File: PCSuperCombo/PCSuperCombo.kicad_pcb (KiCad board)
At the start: 2 copper layers, 123.3 x 95 mm, 44 parts, among them CN1 DB9 Male, J1 IDE_CONNECTOR, J2 CF Adapter Power, J3 Bus_ISA_8bit, J4 LED, SW1 Options, U1 BIOS FLASH, U10 1.8432 MHz, U2 74HCT245, U3 ATF/GAL16V8x-15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

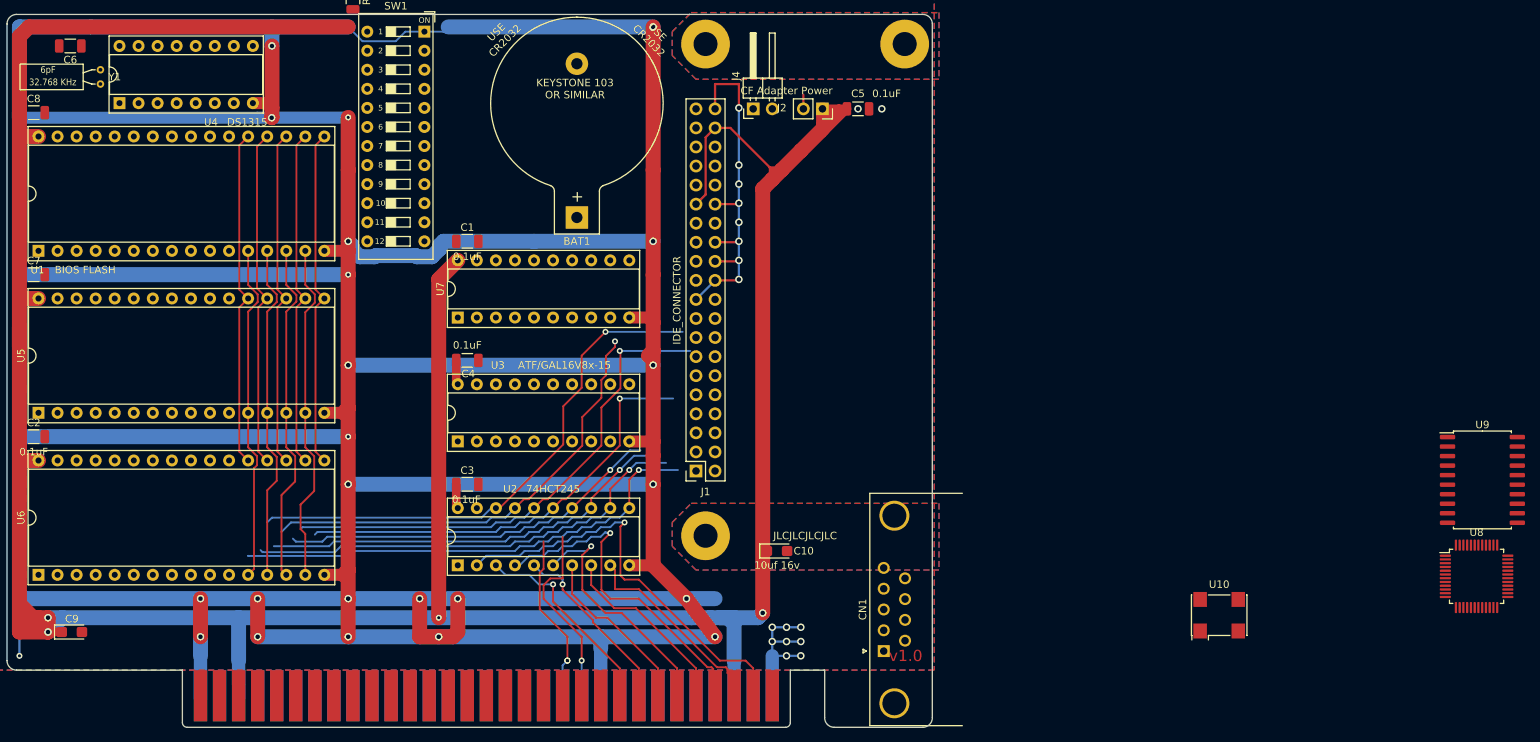
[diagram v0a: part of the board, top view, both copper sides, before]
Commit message: Committing some old edits from mid-2022 to PCSuperCombo. Not sure if these are good changes that should be comitted.
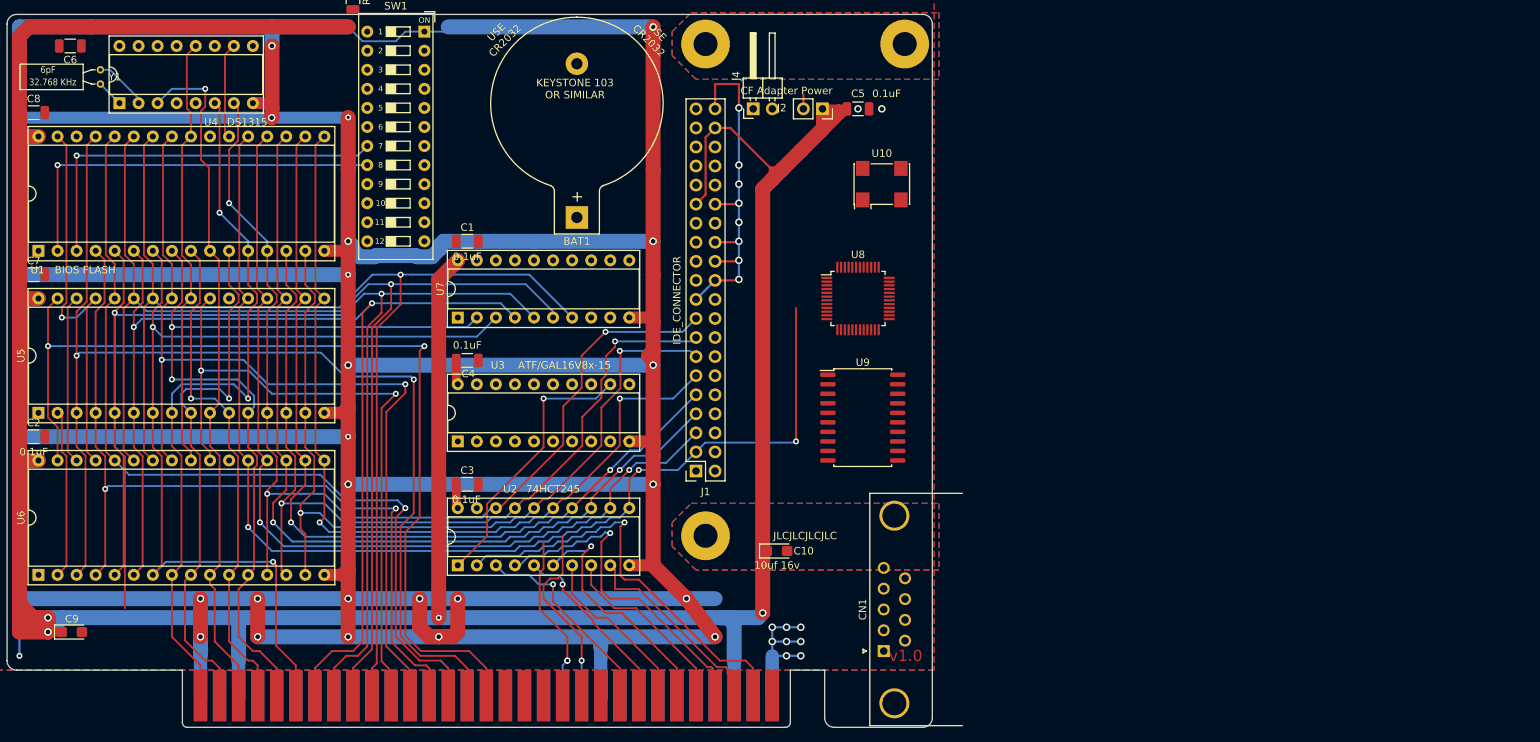
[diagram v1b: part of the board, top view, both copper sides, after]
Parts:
- moved U8 90.4 mm to (186.7, 85.1)
- moved U9 83.0 mm to (187.3, 101.0)
- moved U10 73.0 mm to (189.9, 69.8)
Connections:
- U1 pad 13: Net-(U1-Pad13) -> D0_BUF
- U1 pad 14: Net-(U1-Pad14) -> D1_BUF
- U1 pad 15: Net-(U1-Pad15) -> D2_BUF
- U1 pad 17: Net-(U1-Pad17) -> D3_BUF
- U1 pad 18: Net-(U1-Pad18) -> D4_BUF
- U1 pad 19: Net-(U1-Pad19) -> D5_BUF
- U1 pad 20: Net-(U1-Pad20) -> D6_BUF
- U1 pad 21: Net-(U1-Pad21) -> D7_BUF
- U5 pad 11: A01 -> A03
- U5 pad 12: A00 -> A04
- U5 pad 8: A04 -> A00
- U5 pad 9: A03 -> A01
- U6 pad 11: A01 -> A03
- U6 pad 12: A00 -> A04
- U6 pad 8: A04 -> A00
- U6 pad 9: A03 -> A01
- Y1 pad 1: /XTAL1 -> /XTAL2
- Y1 pad 2: /XTAL2 -> /XTAL1
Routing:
- net A07: track 0.00 -> 200.7 mm, vias 0 -> 2
- net A09: track 0.00 -> 163.4 mm, vias 0 -> 1
- net A08: track 0.25 -> 162.9 mm, vias 0 -> 1
- net A14: track 0.00 -> 156.3 mm, vias 0 -> 2
- net A06: track 0.00 -> 155.1 mm, vias 0 -> 2
- net A15: track 0.00 -> 128.7 mm, vias 0 -> 2
- net A05: track 0.00 -> 128.3 mm, vias 0 -> 2
- net A11: track 0.00 -> 123.0 mm, vias 0 -> 2
- net A13: track 0.00 -> 116.6 mm, vias 0 -> 1
- net A04: track 0.00 -> 115.7 mm, vias 0 -> 2
- net A12: track 0.00 -> 113.5 mm, vias 0 -> 2
- net A02: track 0.00 -> 92.4 mm, vias 0 -> 1
- net A10: track 0.00 -> 91.4 mm, vias 0 -> 2
- net A01: track 0.00 -> 72.4 mm, vias 0 -> 1
- net A03: track 0.00 -> 67.2 mm, vias 0 -> 1
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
